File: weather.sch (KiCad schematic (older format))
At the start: 24 parts, among them J1 Tag-Connect, U1 nRF52810-QCxx, U2 HDC2080, Y1 32MHz, Y2 32kHz

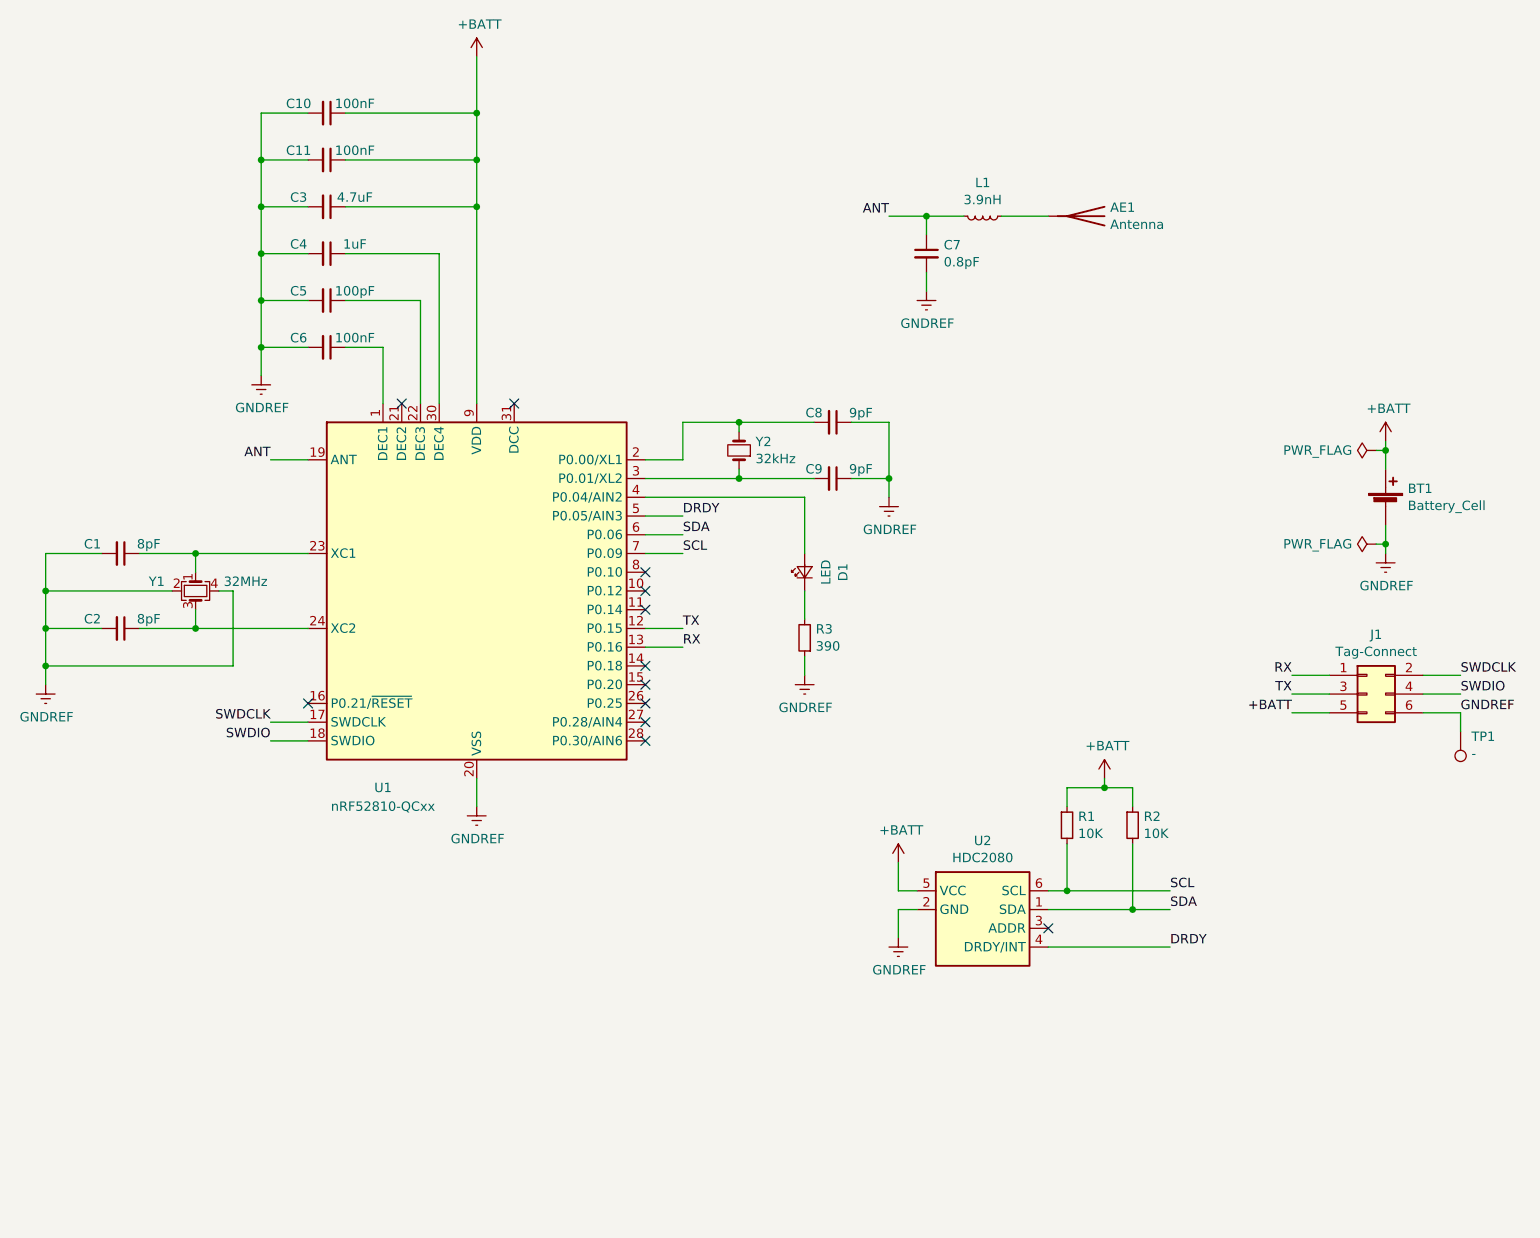
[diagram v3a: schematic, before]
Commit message: Switch to BME680 sensor
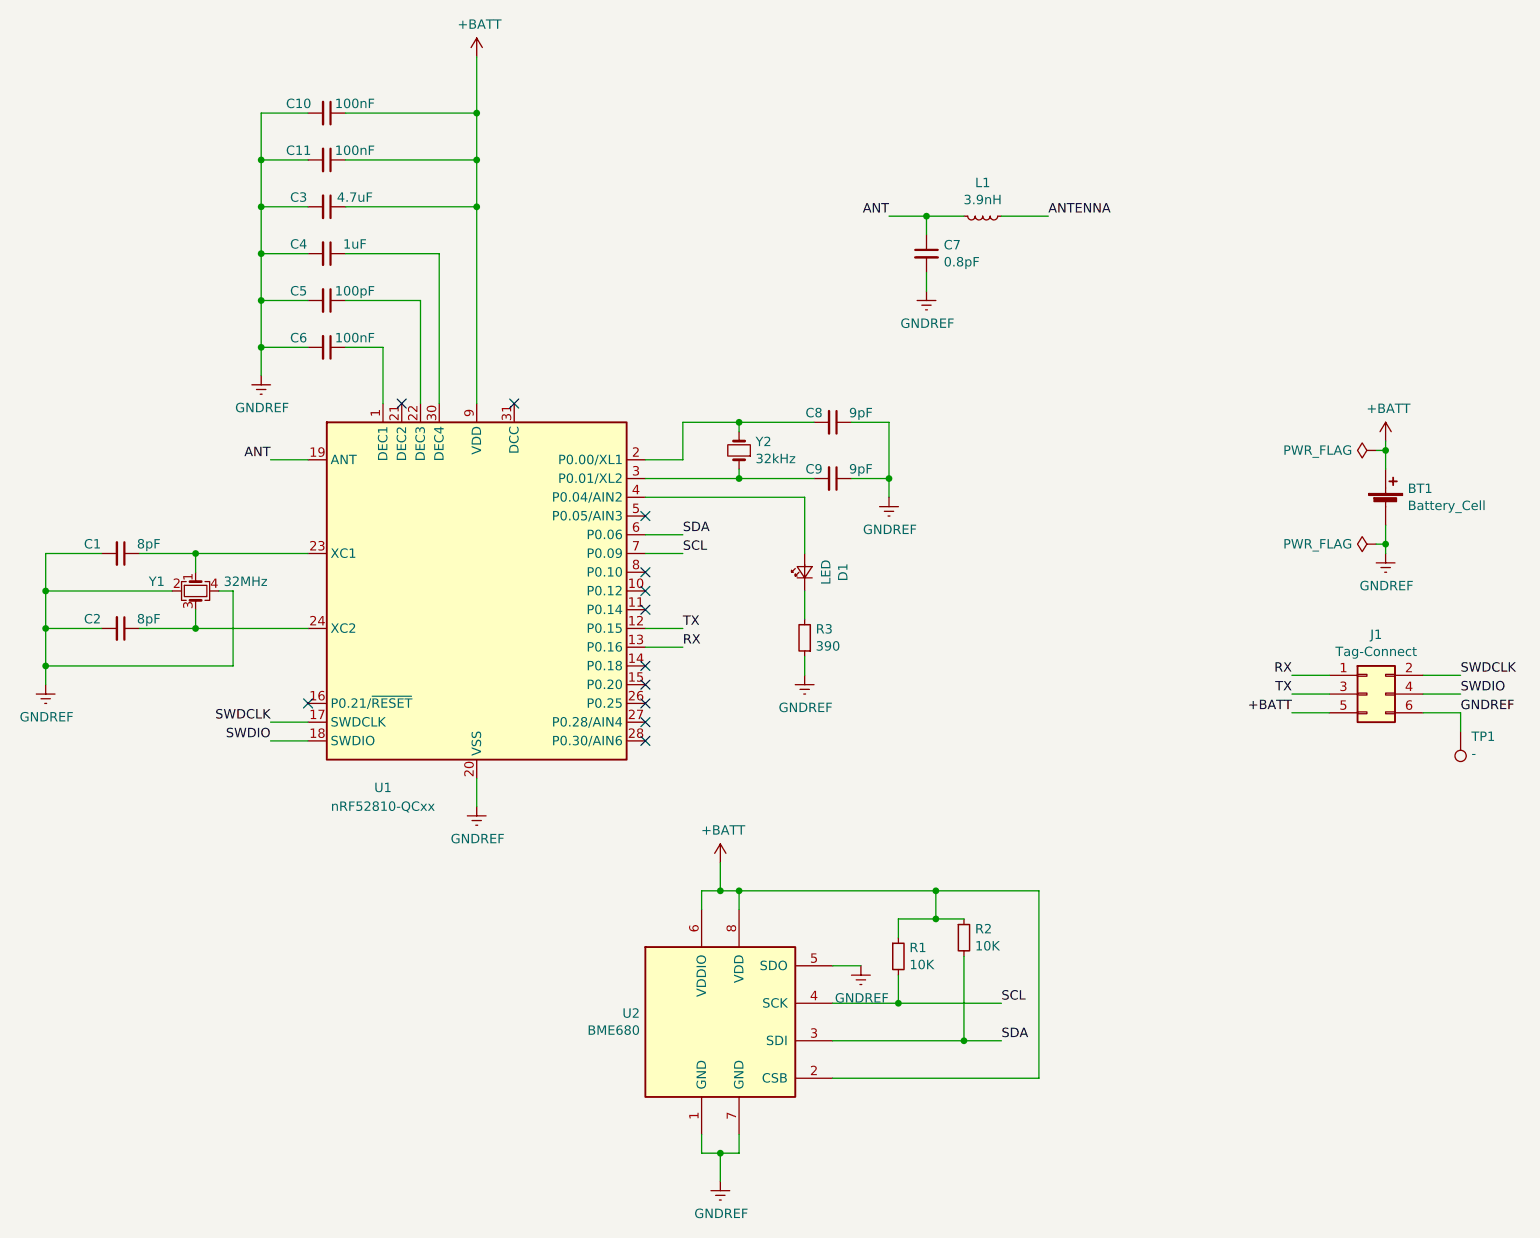
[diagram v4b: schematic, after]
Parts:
- removed AE1: Antenna, NetTie:NetTie-2_SMD_Pad0.5mm, symbol Device:Antenna
- removed U2: HDC2080, Package_SON:Texas_PWSON-N6, symbol Anders_ICs:HDC2080
- added U2: BME680, Package_LGA:Bosch_LGA-8_3x3mm_P0.8mm_ClockwisePinNumbering, symbol Sensor:BME680
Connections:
- net +BATT: now also U2.2 (CSB), U2.6 (VDDIO), U2.8 (VDD)
- net GNDREF: now also U2.1 (GND), U2.5 (SDO), U2.7 (GND)
- net SCL: now also U2.4 (SCK)
- net SDA: now also U2.3 (SDI)
- net ANTENNA: now reaches L1.1
- net DRDY: no longer names the net of U1.5 (P0.05/AIN3)
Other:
- moved on the sheet: R1, R2
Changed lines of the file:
@@
 Sheet 1 1
 Title ""
-Date "2019-03-29"
-Rev "1.1"
+Date "2019-04-01"
+Rev "1.2"
 Comp ""
 Comment1 ""
@@
 Text Label 4250 4150 0    50   ~ 0
 RX
-Text Label 6850 5450 0    50   ~ 0
+Text Label 5950 6050 0    50   ~ 0
 SCL
-Text Label 6850 5550 0    50   ~ 0
+Text Label 5950 6250 0    50   ~ 0
 SDA
 Wire Wire Line
-	6200 5450 6300 5450
-Wire Wire Line
-	6200 5550 6650 5550
+	5050 6050 5400 6050
 $Comp
 L power:GNDREF #PWR0104
 U 1 1 5B7F3B6B
-P 5400 5700
-F 0 "#PWR0104" H 5400 5450 50  0001 C CNN
-F 1 "GNDREF" H 5405 5527 50  0000 C CNN
-F 2 "" H 5400 5700 50  0001 C CNN
-F 3 "" H 5400 5700 50  0001 C CNN
-	1    5400 5700
-	1    0    0    -1
-$EndComp
-Wire Wire Line
-	5400 5550 5400 5700
+P 4450 7000
+F 0 "#PWR0104" H 4450 6750 50  0001 C CNN
+F 1 "GNDREF" H 4455 6827 50  0000 C CNN
+F 2 "" H 4450 7000 50  0001 C CNN
+F 3 "" H 4450 7000 50  0001 C CNN
+	1    4450 7000
+	1    0    0    -1
+$EndComp
 $Comp
 L power:GNDREF #PWR0105
@@
 L power:+BATT #PWR0107
 U 1 1 5B7FB9F7
-P 5400 5300
-F 0 "#PWR0107" H 5400 5150 50  0001 C CNN
-F 1 "+BATT" H 5415 5473 50  0000 C CNN
-F 2 "" H 5400 5300 50  0001 C CNN
-F 3 "" H 5400 5300 50  0001 C CNN
-	1    5400 5300
+P 4450 5300
+F 0 "#PWR0107" H 4450 5150 50  0001 C CNN
+F 1 "+BATT" H 4465 5473 50  0000 C CNN
+F 2 "" H 4450 5300 50  0001 C CNN
+F 3 "" H 4450 5300 50  0001 C CNN
+	1    4450 5300
 	1    0    0    -1
 $EndComp
@@
 	3150 1000 3150 1300
 Connection ~ 3150 1800
-Wire Wire Line
-	5400 5300 5400 5450
 NoConn ~ 4050 4650
 NoConn ~ 4050 4550
@@
 L Device:R_Small R1
 U 1 1 5B7EBF9A
-P 6300 5100
-F 0 "R1" H 6359 5146 50  0000 L CNN
-F 1 "10K" H 6359 5055 50  0000 L CNN
-F 2 "Resistor_SMD:R_0603_1608Metric" H 6300 5100 50  0001 C CNN
-F 3 "~" H 6300 5100 50  0001 C CNN
-	1    6300 5100
+P 5400 5800
+F 0 "R1" H 5459 5846 50  0000 L CNN
+F 1 "10K" H 5459 5755 50  0000 L CNN
+F 2 "Resistor_SMD:R_0603_1608Metric" H 5400 5800 50  0001 C CNN
+F 3 "~" H 5400 5800 50  0001 C CNN
+	1    5400 5800
 	1    0    0    -1
 $EndComp
@@
 L Device:R_Small R2
 U 1 1 5B7ECE35
-P 6650 5100
-F 0 "R2" H 6709 5146 50  0000 L CNN
-F 1 "10K" H 6709 5055 50  0000 L CNN
-F 2 "Resistor_SMD:R_0603_1608Metric" H 6650 5100 50  0001 C CNN
-F 3 "~" H 6650 5100 50  0001 C CNN
-	1    6650 5100
-	1    0    0    -1
-$EndComp
-$Comp
-L power:+BATT #PWR0110
-U 1 1 5B7ECEF8
-P 6500 4850
-F 0 "#PWR0110" H 6500 4700 50  0001 C CNN
-F 1 "+BATT" H 6515 5023 50  0000 C CNN
-F 2 "" H 6500 4850 50  0001 C CNN
-F 3 "" H 6500 4850 50  0001 C CNN
-	1    6500 4850
-	1    0    0    -1
-$EndComp
-Wire Wire Line
-	6300 5000 6300 4900
-Wire Wire Line
-	6300 4900 6500 4900
-Wire Wire Line
-	6500 4900 6500 4850
-Wire Wire Line
-	6650 5000 6650 4900
-Wire Wire Line
-	6650 4900 6500 4900
-Connection ~ 6500 4900
-Wire Wire Line
-	6300 5200 6300 5450
-Connection ~ 6300 5450
-Wire Wire Line
-	6300 5450 6850 5450
-Wire Wire Line
-	6650 5200 6650 5550
-Connection ~ 6650 5550
-Wire Wire Line
-	6650 5550 6850 5550
+P 5750 5700
+F 0 "R2" H 5809 5746 50  0000 L CNN
+F 1 "10K" H 5809 5655 50  0000 L CNN
+F 2 "Resistor_SMD:R_0603_1608Metric" H 5750 5700 50  0001 C CNN
+F 3 "~" H 5750 5700 50  0001 C CNN
+	1    5750 5700
+	1    0    0    -1
+$EndComp
+Wire Wire Line
+	5400 5700 5400 5600
+Wire Wire Line
+	5400 5900 5400 6050
+Connection ~ 5400 6050
+Wire Wire Line
+	5400 6050 5950 6050
+Wire Wire Line
+	5750 5800 5750 6250
+Connection ~ 5750 6250
+Wire Wire Line
+	5750 6250 5950 6250
 $Comp
 L Device:Crystal_Small Y2
@@
 Wire Wire Line
 	3150 1550 3150 1800
-$Comp
-L Device:Antenna AE1
-U 1 1 5B85E789
-P 6400 1850
-F 0 "AE1" V 6354 1980 50  0000 L CNN
-F 1 "Antenna" V 6445 1980 50  0000 L CNN
-F 2 "NetTie:NetTie-2_SMD_Pad0.5mm" H 6400 1850 50  0001 C CNN
-F 3 "~" H 6400 1850 50  0001 C CNN
-	1    6400 1850
-	0    1    1    0
-$EndComp
 Wire Wire Line
 	5550 2150 5550 2250
@@
 	4900 3850 4900 4000
 Wire Wire Line
-	5400 5450 5500 5450
-Wire Wire Line
-	5400 5550 5500 5550
-NoConn ~ 6200 5650
-Wire Wire Line
 	4050 3250 4550 3250
 Wire Wire Line
 	4250 2950 4250 3150
-Text Label 4250 3450 0    50   ~ 0
-DRDY
-Wire Wire Line
-	4250 3450 4050 3450
-Text Label 6850 5750 0    50   ~ 0
-DRDY
-Wire Wire Line
-	6850 5750 6200 5750
-$Comp
-L Anders_ICs:HDC2080 U2
-U 1 1 5BBE39A8
-P 5850 5600
-F 0 "U2" H 5850 6017 50  0000 C CNN
-F 1 "HDC2080" H 5850 5926 50  0000 C CNN
-F 2 "Package_SON:Texas_PWSON-N6" H 5850 5300 50  0001 L CNN
-F 3 "http://www.ti.com/lit/ds/symlink/hdc2080.pdf" H 5500 5900 50  0001 C CNN
-	1    5850 5600
-	1    0    0    -1
-$EndComp
+$Comp
+L Sensor:BME680 U2
+U 1 1 5CAF7E91
+P 4450 6150
+F 0 "U2" H 4021 6196 50  0000 R CNN
+F 1 "BME680" H 4021 6105 50  0000 R CNN
+F 2 "Package_LGA:Bosch_LGA-8_3x3mm_P0.8mm_ClockwisePinNumbering" H 4450 5950 50  0001 C CNN
+F 3 "https://ae-bst.resource.bosch.com/media/_tech/media/datasheets/BST-BME680-DS001-00.pdf" H 4450 5950 50  0001 C CNN
+	1    4450 6150
+	1    0    0    -1
+$EndComp
+Wire Wire Line
+	5050 6450 6150 6450
+$Comp
+L power:GNDREF #PWR0110
+U 1 1 5CAFC6F2
+P 5200 5850
+F 0 "#PWR0110" H 5200 5600 50  0001 C CNN
+F 1 "GNDREF" H 5205 5677 50  0000 C CNN
+F 2 "" H 5200 5850 50  0001 C CNN
+F 3 "" H 5200 5850 50  0001 C CNN
+	1    5200 5850
+	1    0    0    -1
+$EndComp
+Wire Wire Line
+	5050 5850 5200 5850
+Wire Wire Line
+	4350 6750 4350 6850
+Wire Wire Line
+	4350 6850 4450 6850
+Wire Wire Line
+	4450 6850 4450 7000
+Wire Wire Line
+	4550 6750 4550 6850
+Wire Wire Line
+	4550 6850 4450 6850
+Connection ~ 4450 6850
+Wire Wire Line
+	4350 5550 4350 5450
+Wire Wire Line
+	4350 5450 4450 5450
+Wire Wire Line
+	4550 5450 4550 5550
+Wire Wire Line
+	4450 5300 4450 5450
+Connection ~ 4450 5450
+Wire Wire Line
+	4450 5450 4550 5450
+Wire Wire Line
+	6150 5450 5600 5450
+Wire Wire Line
+	6150 5450 6150 6450
+Connection ~ 4550 5450
+Wire Wire Line
+	5050 6250 5750 6250
+Wire Wire Line
+	5400 5600 5600 5600
+Wire Wire Line
+	5600 5600 5600 5450
+Connection ~ 5600 5600
+Wire Wire Line
+	5600 5600 5750 5600
+Connection ~ 5600 5450
+Wire Wire Line
+	5600 5450 4550 5450
+NoConn ~ 4050 3450
+Text Label 6200 1850 0    50   ~ 0
+ANTENNA
 $EndSCHEMATC
